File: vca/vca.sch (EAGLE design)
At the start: 52 parts, among them IC1 OPA4130U, IC2 OPA134D, Q1 BC847ALT1SMD, X1 2516-

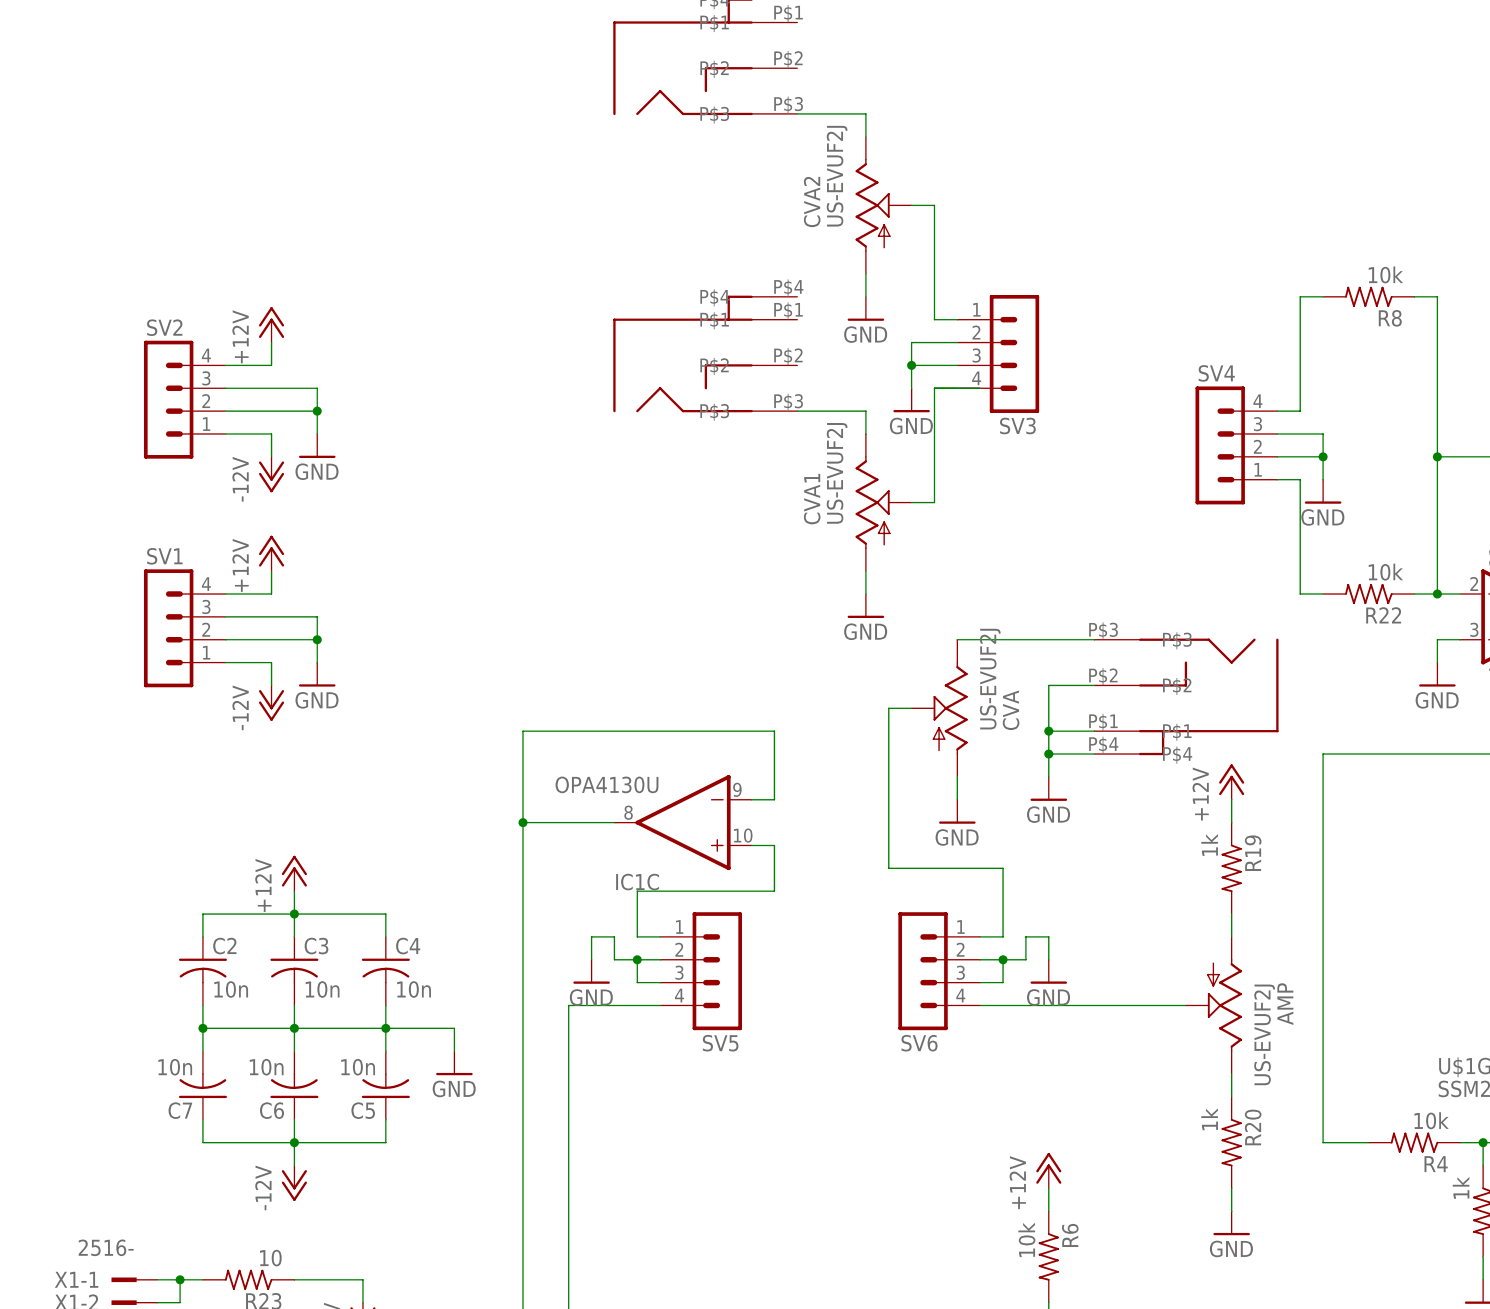
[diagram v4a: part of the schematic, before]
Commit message: finished the vca.  more or less ready.
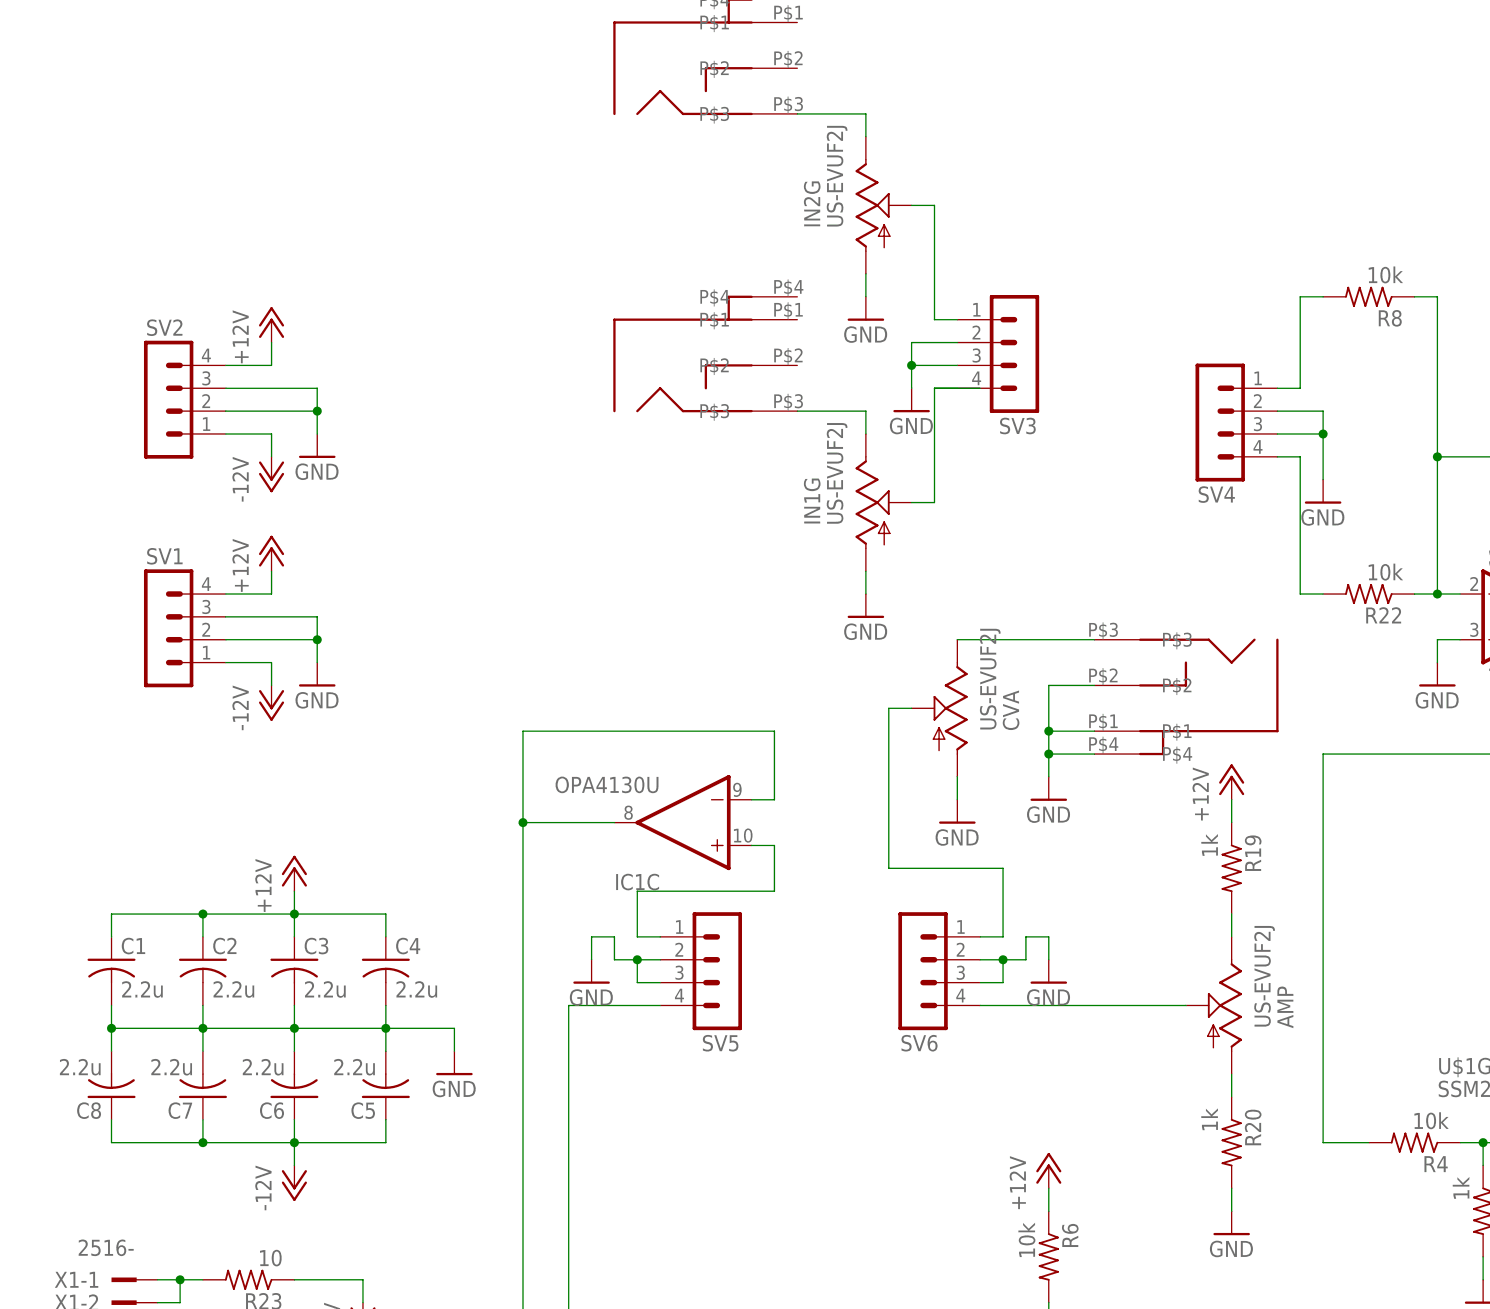
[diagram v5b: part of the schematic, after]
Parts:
- added C1, C8: 2.2u, dan:C-USC0603
- C2, C3, C4, C5, C6, C7: value 10n -> 2.2u
- renumbered CVA1 to IN1G, CVA2 to IN2G
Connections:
- net +12V: now also C1.1
- net -12V: now also C8.1
- net GND: now also C1.2, C8.2
- net N$22: now also AMP.E; no longer AMP.A
- net N$23: now also AMP.A; no longer AMP.E
- net N$28: now also SV4.1; no longer SV4.4
- net N$29: now also SV4.4; no longer SV4.1
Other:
- moved on the sheet: AMP, SV4

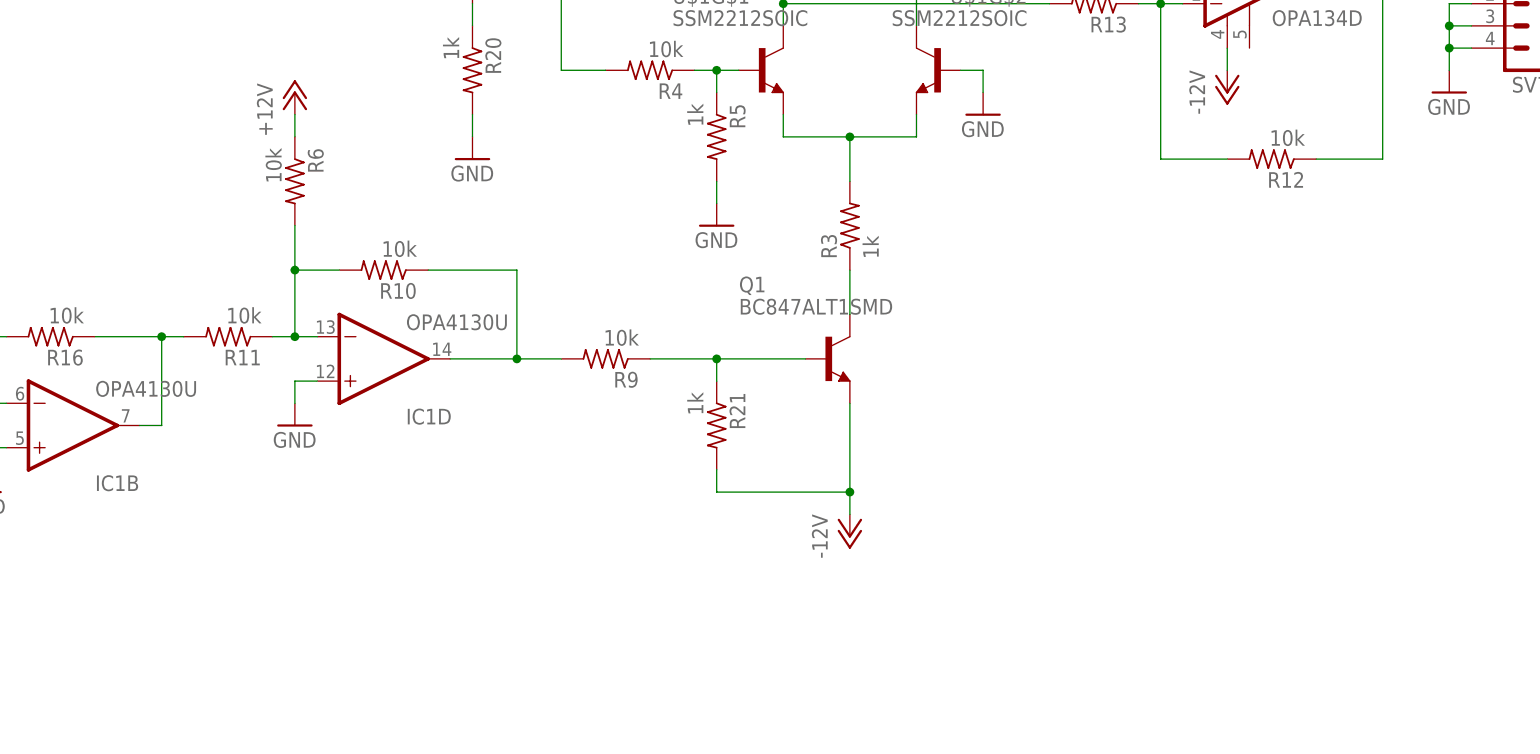
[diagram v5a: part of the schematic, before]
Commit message: finished vca.  probably needs a series protection resistor on output.
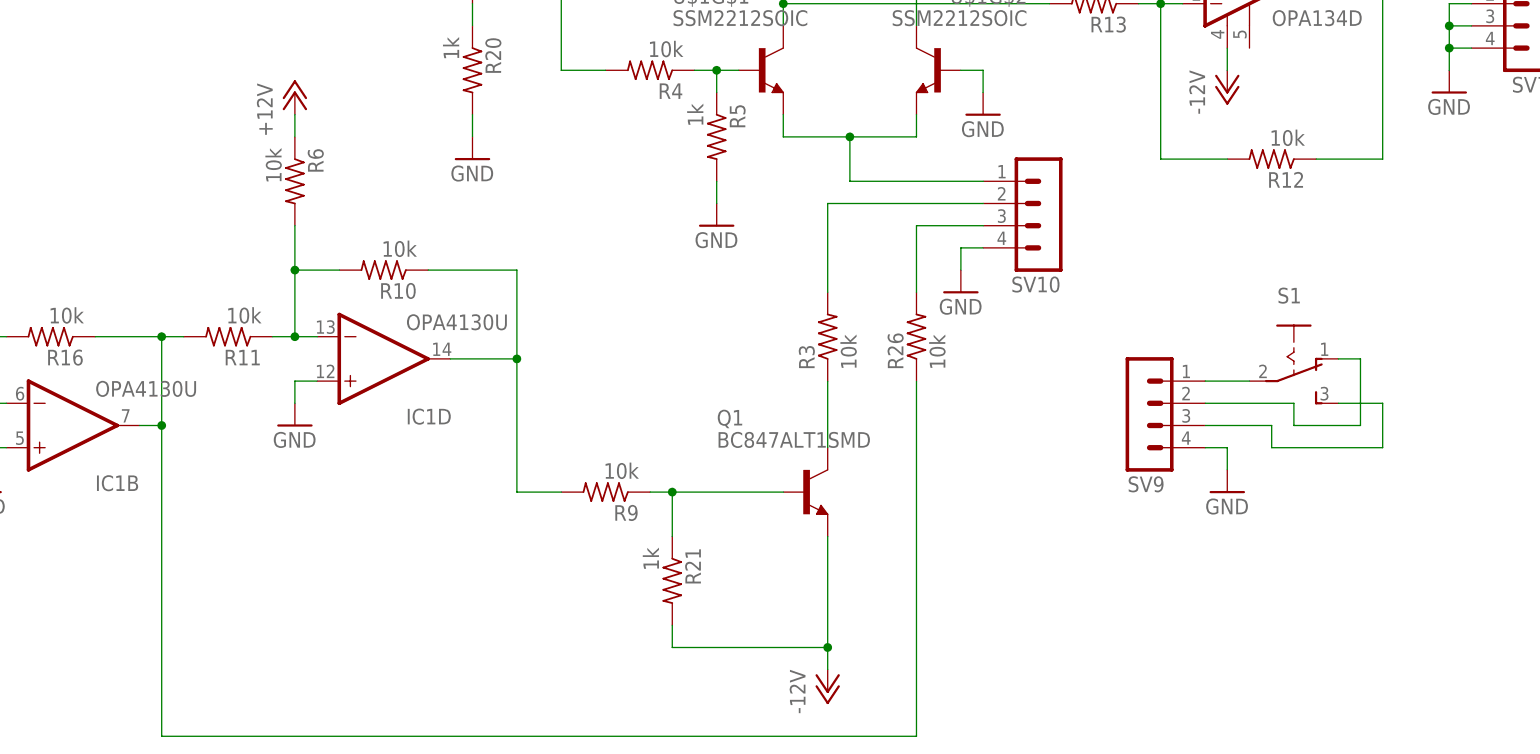
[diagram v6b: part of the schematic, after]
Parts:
- added R26: 10k, dan:R-US_R0603
- added S1: (no value), dan:255SB
- added SV10, SV9: (no value), dan:MA04-1
- R3: value 1k -> 10k
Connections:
- removed net N$17: IC1B.OUT, R11.2, R16.1
- new net N$35: R3.2, SV10.2
- new net N$36: IC1B.OUT, R11.2, R16.1, R26.1
- new net N$37: S1.P, SV9.1
- new net N$38: R26.2, SV10.3
- new net N$40: S1.O, SV9.2
- new net N$41: S1.S, SV9.3
- net GND: now also SV10.4, SV9.4
- net N$1: now also SV10.1; no longer R3.2
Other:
- moved on the sheet: Q1, R21, R3, R9

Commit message: made a couple post fab vca changes
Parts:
- added R25: 1Meg, dan:R-US_R0603
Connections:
- net GND: now also IN1.P$1, IN1.P$2, IN1.P$4, IN2.P$1, IN2.P$2, IN2.P$4, R25.1
- net N$12: now also R25.2
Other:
- note added: "Fixed missing grounds here"
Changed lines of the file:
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@@
 <part name="GND23" library="dan" deviceset="GND" device=""/>
 <part name="GND24" library="dan" deviceset="GND" device=""/>
+<part name="GND25" library="dan" deviceset="GND" device=""/>
+<part name="GND26" library="dan" deviceset="GND" device=""/>
+<part name="R25" library="dan" deviceset="R-US_" device="R0603" value="1Meg"/>
+<part name="GND27" library="dan" deviceset="GND" device=""/>
 </parts>
 <sheets>
 <sheet>
 <plain>
+<text x="-58.42" y="170.18" size="1.778" layer="91">Fixed missing grounds here</text>
 </plain>
 <instances>
@@
 <instance part="R21" gate="G$1" x="10.16" y="-12.7" rot="R270"/>
 <instance part="P-7" gate="1" x="27.94" y="-25.4"/>
-<instance part="IN1" gate="G$1" x="-71.12" y="132.08"/>
+<instance part="IN1" gate="G$1" x="-78.74" y="132.08"/>
 <instance part="IN1G" gate="G$1" x="-53.34" y="116.84"/>
 <instance part="GND2" gate="1" x="10.16" y="96.52"/>
@@
 <instance part="R22" gate="G$1" x="2.54" y="106.68" rot="R180"/>
 <instance part="GND14" gate="1" x="-53.34" y="104.14"/>
-<instance part="IN2" gate="G$1" x="-71.12" y="165.1"/>
+<instance part="IN2" gate="G$1" x="-78.74" y="165.1"/>
 <instance part="IN2G" gate="G$1" x="-53.34" y="149.86"/>
 <instance part="GND15" gate="1" x="-53.34" y="137.16"/>
@@
 <instance part="GND23" gate="1" x="43.18" y="20.32"/>
 <instance part="GND24" gate="1" x="73.66" y="-2.54"/>
+<instance part="GND25" gate="1" x="-60.96" y="165.1"/>
+<instance part="GND26" gate="1" x="-60.96" y="132.08"/>
+<instance part="R25" gate="G$1" x="-45.72" y="33.02" rot="R270"/>
+<instance part="GND27" gate="1" x="-53.34" y="35.56"/>
 </instances>
 <busses>
@@
 <wire x1="73.66" y1="2.54" x2="73.66" y2="0" width="0.1524" layer="91"/>
 </segment>
+<segment>
+<pinref part="GND26" gate="1" pin="GND"/>
+<wire x1="-60.96" y1="134.62" x2="-60.96" y2="139.7" width="0.1524" layer="91"/>
+<pinref part="IN1" gate="G$1" pin="P$2"/>
+<wire x1="-68.58" y1="132.08" x2="-66.04" y2="132.08" width="0.1524" layer="91"/>
+<wire x1="-66.04" y1="132.08" x2="-66.04" y2="137.16" width="0.1524" layer="91"/>
+<pinref part="IN1" gate="G$1" pin="P$4"/>
+<wire x1="-66.04" y1="137.16" x2="-66.04" y2="139.7" width="0.1524" layer="91"/>
+<wire x1="-66.04" y1="139.7" x2="-68.58" y2="139.7" width="0.1524" layer="91"/>
+<wire x1="-60.96" y1="139.7" x2="-66.04" y2="139.7" width="0.1524" layer="91"/>
+<pinref part="IN1" gate="G$1" pin="P$1"/>
+<wire x1="-68.58" y1="137.16" x2="-66.04" y2="137.16" width="0.1524" layer="91"/>
+<junction x="-66.04" y="137.16"/>
+<junction x="-66.04" y="139.7"/>
+</segment>
+<segment>
+<pinref part="IN2" gate="G$1" pin="P$4"/>
+<pinref part="GND25" gate="1" pin="GND"/>
+<wire x1="-68.58" y1="172.72" x2="-66.04" y2="172.72" width="0.1524" layer="91"/>
+<wire x1="-66.04" y1="172.72" x2="-60.96" y2="172.72" width="0.1524" layer="91"/>
+<wire x1="-60.96" y1="172.72" x2="-60.96" y2="167.64" width="0.1524" layer="91"/>
+<pinref part="IN2" gate="G$1" pin="P$1"/>
+<wire x1="-68.58" y1="170.18" x2="-66.04" y2="170.18" width="0.1524" layer="91"/>
+<wire x1="-66.04" y1="170.18" x2="-66.04" y2="172.72" width="0.1524" layer="91"/>
+<pinref part="IN2" gate="G$1" pin="P$2"/>
+<wire x1="-68.58" y1="165.1" x2="-66.04" y2="165.1" width="0.1524" layer="91"/>
+<wire x1="-66.04" y1="165.1" x2="-66.04" y2="170.18" width="0.1524" layer="91"/>
+<junction x="-66.04" y="170.18"/>
+<junction x="-66.04" y="172.72"/>
+</segment>
+<segment>
+<pinref part="R25" gate="G$1" pin="1"/>
+<wire x1="-45.72" y1="38.1" x2="-45.72" y2="40.64" width="0.1524" layer="91"/>
+<wire x1="-45.72" y1="40.64" x2="-53.34" y2="40.64" width="0.1524" layer="91"/>
+<pinref part="GND27" gate="1" pin="GND"/>
+<wire x1="-53.34" y1="40.64" x2="-53.34" y2="38.1" width="0.1524" layer="91"/>
+</segment>
 </net>
 <net name="+12V" class="0">
@@
 <wire x1="-33.02" y1="27.94" x2="-33.02" y2="22.86" width="0.1524" layer="91"/>
 <junction x="-33.02" y="22.86"/>
+<pinref part="R25" gate="G$1" pin="2"/>
+<wire x1="-33.02" y1="22.86" x2="-45.72" y2="22.86" width="0.1524" layer="91"/>
+<wire x1="-45.72" y1="22.86" x2="-45.72" y2="27.94" width="0.1524" layer="91"/>
 </segment>
 </net>
@@
 <segment>
 <pinref part="IN1" gate="G$1" pin="P$3"/>
-<wire x1="-60.96" y1="127" x2="-53.34" y2="127" width="0.1524" layer="91"/>
+<wire x1="-68.58" y1="127" x2="-53.34" y2="127" width="0.1524" layer="91"/>
 <pinref part="IN1G" gate="G$1" pin="E"/>
 <wire x1="-53.34" y1="127" x2="-53.34" y2="124.46" width="0.1524" layer="91"/>
@@
 <segment>
 <pinref part="IN2" gate="G$1" pin="P$3"/>
-<wire x1="-60.96" y1="160.02" x2="-53.34" y2="160.02" width="0.1524" layer="91"/>
+<wire x1="-68.58" y1="160.02" x2="-53.34" y2="160.02" width="0.1524" layer="91"/>
 <pinref part="IN2G" gate="G$1" pin="E"/>
 <wire x1="-53.34" y1="160.02" x2="-53.34" y2="157.48" width="0.1524" layer="91"/>

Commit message: sent out vca again
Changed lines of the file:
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@@
-</segment>
-<segment>
-<wire x1="-40.64" y1="129.54" x2="-45.72" y2="129.54" width="0.1524" layer="91"/>
 </segment>
 <segment>
@@
 <pinref part="P+3" gate="1" pin="+12V"/>
 <wire x1="30.48" y1="78.74" x2="30.48" y2="81.28" width="0.1524" layer="91"/>
-<wire x1="30.48" y1="76.2" x2="30.48" y2="78.74" width="0.1524" layer="91"/>
 </segment>
 <segment>
